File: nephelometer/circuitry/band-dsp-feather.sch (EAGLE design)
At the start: 63 parts, among them IC1 LM4041CILP, IC2 AD822N, IC3 MCP6S21, IC4 LP2950ACZ-3.3, J1 RJ11-6PTH, Q1 IRLB8721, T1 2N2222, T2 2N2222, T3 2N2222, T4 2N2222, T5 2N2222, T6 2N2222

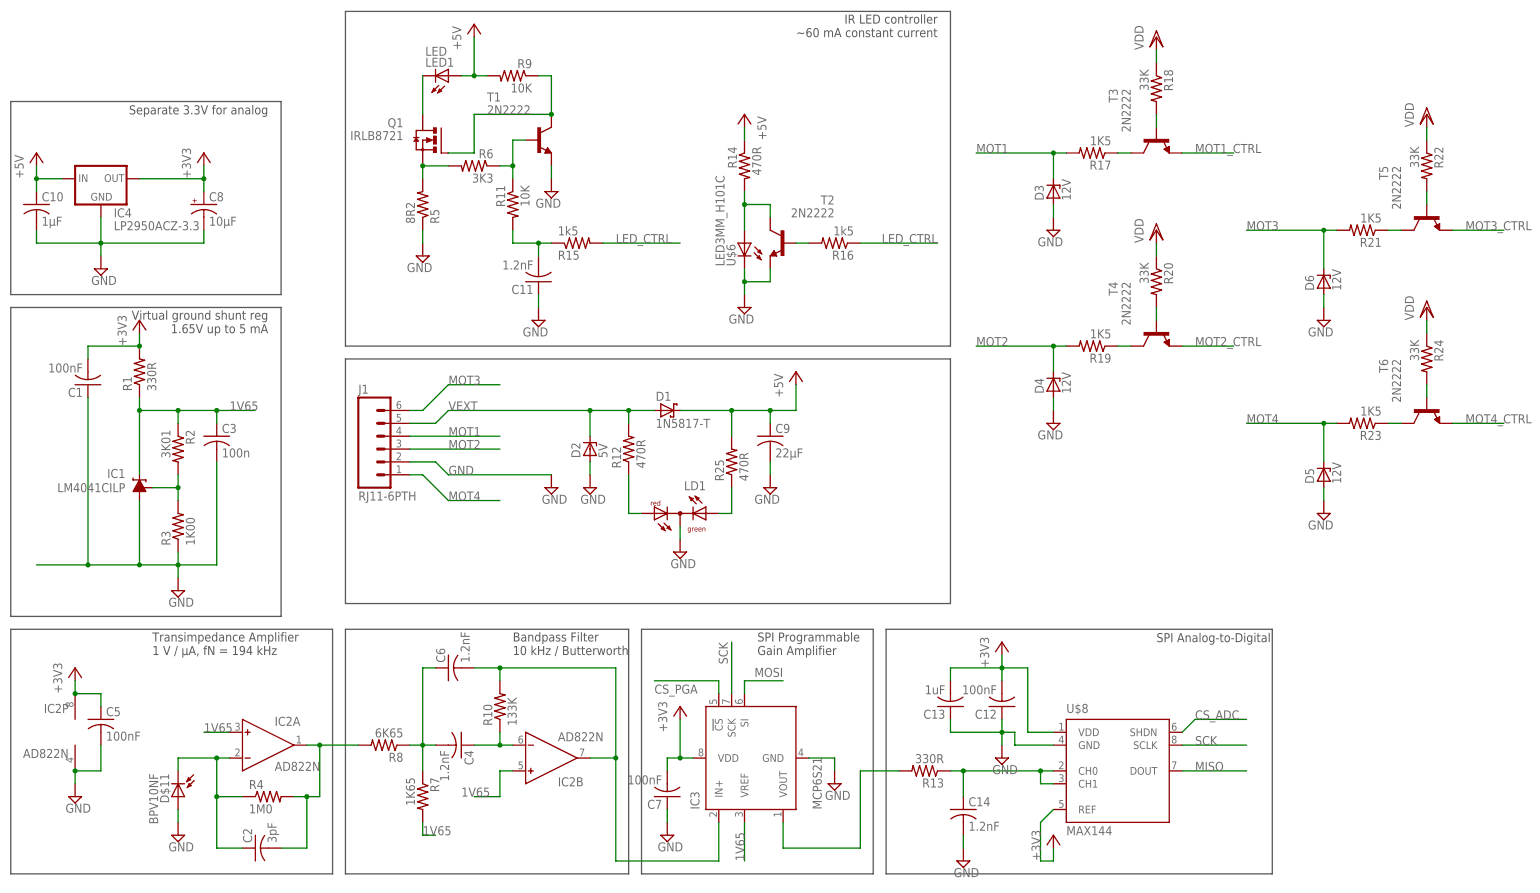
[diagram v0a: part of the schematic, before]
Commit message: Finalized Feather nephelometer with separate ADC and 4 robust motor controls
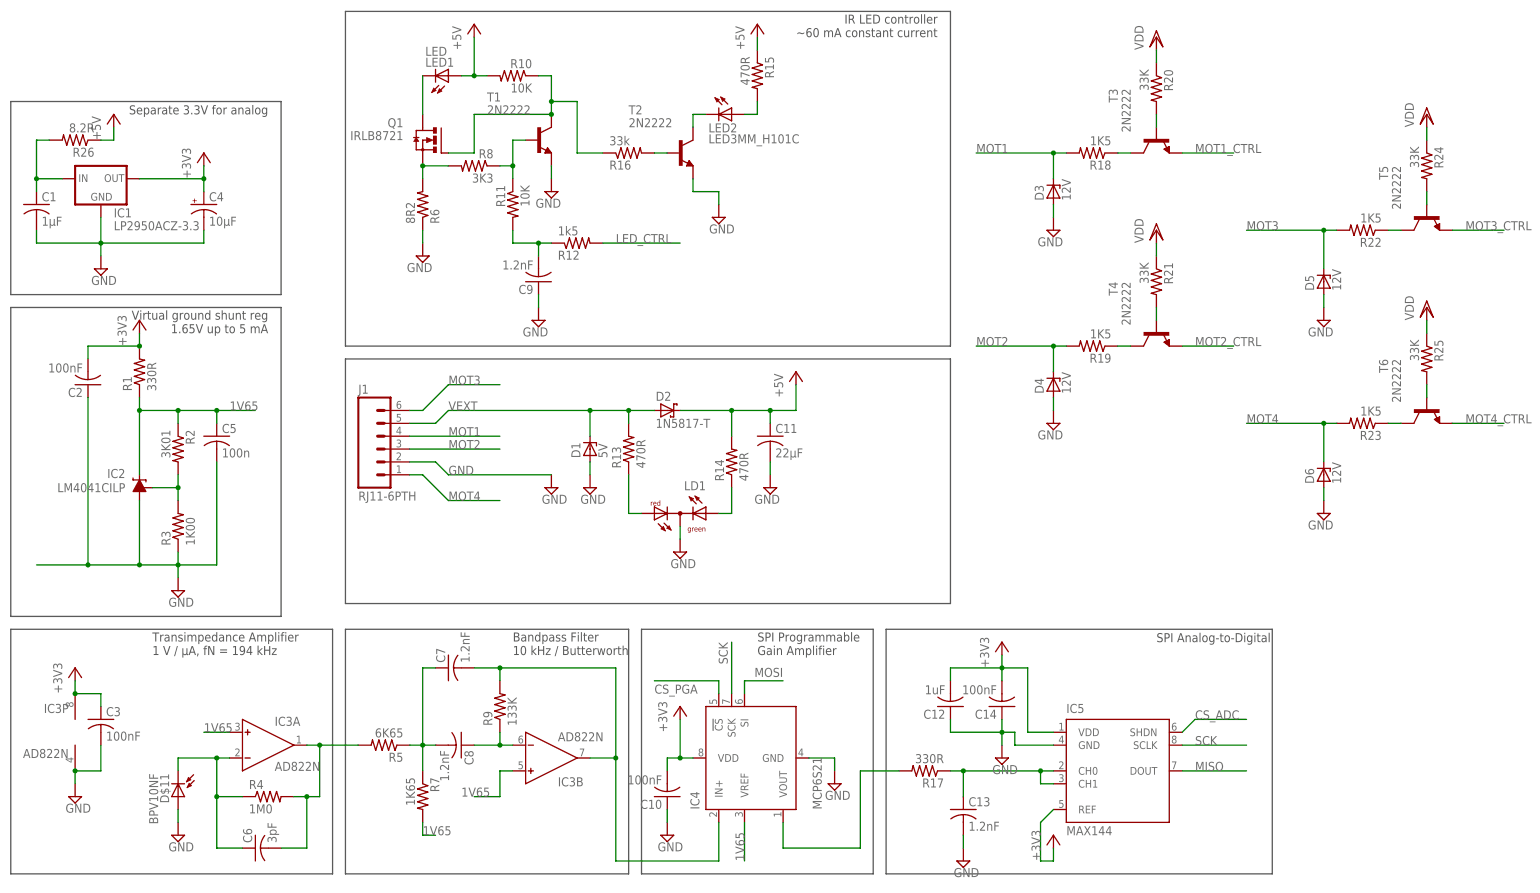
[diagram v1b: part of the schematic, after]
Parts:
- removed U$6: LED3MM_H101C, ingolia:LED3MM_H101C
- added LED2: LED3MM_H101C, ingolia:LED3MM_H101C
- added R26: 8.2R, adafruit:R-US_0207/9
- C1: value 100nF -> 1µF; device adafruit:C-US025-025X050 -> adafruit:C-US025-030X050; DIGIKEY# BC1084CT-ND -> 445-5318-ND; MANF Vishay BC Components -> TDK Corporation; MANF# K104K15X7RF5TL2 -> FK14X7R1C105K
- C10: value 1µF -> 100nF; device adafruit:C-US025-030X050 -> adafruit:C-US025-025X050; DIGIKEY# 445-5318-ND -> BC1084CT-ND; MANF TDK Corporation -> Vishay BC Components; MANF# FK14X7R1C105K -> K104K15X7RF5TL2
- C11: value 1.2nF -> 22µF; device adafruit:C-US025-025X050 -> adafruit:C-US050-045X075; DIGIKEY# BC1026CT-ND -> 445-8455-ND; MANF Vishay BC Components -> TDK Corporation; MANF# K122J15C0GF5TL2 -> FK20X7R1C226M
- C12: value 100nF -> 1uF; DIGIKEY# BC1084CT-ND -> 445-5318-ND; MANF Vishay BC Components -> TDK Corporation; MANF# K104K15X7RF5TL2 -> FK14X7R1C105K
- C13: value 1uF -> 1.2nF; DIGIKEY# BC1084CT-ND -> BC1026CT-ND; MANF# K104K15X7RF5TL2 -> K122J15C0GF5TL2
- C14: value 1.2nF -> 100nF; DIGIKEY# BC1026CT-ND -> BC1084CT-ND; MANF# K122J15C0GF5TL2 -> K104K15X7RF5TL2
- C2: value 3pF -> 100nF; device adafruit:C-US025-024X044 -> adafruit:C-US025-025X050; DIGIKEY# 445-8377-ND -> BC1084CT-ND; MANF TDK Corporation -> Vishay BC Components; MANF# FK18C0G1H030C -> K104K15X7RF5TL2
- C3: value 100n -> 100nF
- C4: value 1.2nF -> 10µF; device adafruit:C-US025-025X050 -> adafruit:CPOL-USE2.5-5; DIGIKEY# BC1026CT-ND -> 478-8042-1-ND; MANF Vishay BC Components -> AVX Corporation; MANF# K122J15C0GF5TL2 -> TAP106K016SRW
- C5: value 100nF -> 100n
- C6: value 1.2nF -> 3pF; device adafruit:C-US025-025X050 -> adafruit:C-US025-024X044; DIGIKEY# BC1026CT-ND -> 445-8377-ND; MANF Vishay BC Components -> TDK Corporation; MANF# K122J15C0GF5TL2 -> FK18C0G1H030C
- C7: value 100nF -> 1.2nF; DIGIKEY# BC1084CT-ND -> BC1026CT-ND; MANF# K104K15X7RF5TL2 -> K122J15C0GF5TL2
- C8: value 10µF -> 1.2nF; device adafruit:CPOL-USE2.5-5 -> adafruit:C-US025-025X050; DIGIKEY# 478-8042-1-ND -> BC1026CT-ND; MANF AVX Corporation -> Vishay BC Components; MANF# TAP106K016SRW -> K122J15C0GF5TL2
- C9: value 22µF -> 1.2nF; device adafruit:C-US050-045X075 -> adafruit:C-US025-025X050; DIGIKEY# 445-8455-ND -> BC1026CT-ND; MANF TDK Corporation -> Vishay BC Components; MANF# FK20X7R1C226M -> K122J15C0GF5TL2
- D1: value 1N5817-T -> 5V; device diode:1N5817-T -> diode:ZENER-DIODEF126-10; DIGIKEY# 1N5817FSCT-ND -> SA5.0ALFCT-ND; MANF Fairchild Semiconductor -> Littelfuse Inc.; MANF# 1N5817 -> SA5.0A
- D2: value 5V -> 1N5817-T; device diode:ZENER-DIODEF126-10 -> diode:1N5817-T; DIGIKEY# (none) -> 1N5817FSCT-ND; MANF (none) -> Fairchild Semiconductor; MANF# (none) -> 1N5817
- D3, D4, D5, D6: DIGIKEY# (none) -> SA12CALFCT-ND; MANF (none) -> Littelfuse Inc.; MANF# (none) -> SA12CA
- IC1: value LM4041CILP -> LP2950ACZ-3.3; device texas:LM4041CILP -> v-reg:LP2950ACZ-3.3; DIGIKEY# 296-22173-1-ND -> LP2950ACZ-3.3/NOPB-ND; MANF# LM4041CILPR -> LP2950ACZ-3.3/NOPB
- IC2: value AD822N -> LM4041CILP; device analog-devices:AD822N -> texas:LM4041CILP; DIGIKEY# AD823ANZ-ND -> 296-22173-1-ND; MANF Analog Devices Inc. -> Texas Instruments; MANF# AD823ANZ -> LM4041CILPR
- IC3: value MCP6S21 -> AD822N; device ingolia:MCP6S21 -> analog-devices:AD822N; DIGIKEY# MCP6S91-E/P-ND -> AD823ANZ-ND; MANF Microchip Technology -> Analog Devices Inc.; MANF# MCP6S91-E/P -> AD823ANZ
- IC4: value LP2950ACZ-3.3 -> MCP6S21; device v-reg:LP2950ACZ-3.3 -> ingolia:MCP6S21; DIGIKEY# LP2950ACZ-3.3/NOPB-ND -> MCP6S91-E/P-ND; MANF Texas Instruments -> Microchip Technology; MANF# LP2950ACZ-3.3/NOPB -> MCP6S91-E/P
- IC5: DIGIKEY# (none) -> MAX144ACPA+-ND; MANF (none) -> Maxim Integrated; MANF# (none) -> MAX144ACPA+
- IC6: DIGIKEY# (none) -> 1528-1531-ND; DIGIKEY2# (none) -> 2830-ND; MANF (none) -> Adafruit Industries LLC; MANF# (none) -> 2772; MANF2 (none) -> Adafruit Industries LLC; MANF2# (none) -> 2830
- LD1: DIGIKEY# (none) -> 754-1221-ND; MANF (none) -> Kingbright; MANF# (none) -> WP3VEGW
- R10: value 133K -> 10K; DIGIKEY# 133KXBK-ND -> CF14JT10K0CT-ND; MANF Yageo -> Stackpole Electronics Inc; MANF# MFR-25FBF52-133K -> CF14JT10K0
- R11: DIGIKEY# CF14JT4K70CT-ND -> CF14JT10K0CT-ND; MANF# CF14JT4K70 -> CF14JT10K0
- R12: value 470R -> 1k5; DIGIKEY# CF14JT330RCT-ND -> CF14JT1K50CT-ND; MANF Stackpole Electronics Inc. -> Stackpole Electronics Inc; MANF# CF14JT330R -> CF14JT1K50
- R13: value 330R -> 470R; DIGIKEY# 6.65KXBK-ND -> CF14JT470RCT-ND; MANF Yageo -> Stackpole Electronics Inc.; MANF# MFR-25FBF52-6K65 -> CF14JT470R
- R14: device adafruit:R-US_0207/5V -> adafruit:R-US_0207/9; DIGIKEY# CF14JT150RCT-ND -> CF14JT470RCT-ND; MANF# CF14JT150R -> CF14JT470R
- R15: value 1k5 -> 470R; device adafruit:R-US_0207/9 -> adafruit:R-US_0207/5V; DIGIKEY# CF14JT4K70CT-ND -> CF14JT470RCT-ND; MANF Stackpole Electronics Inc -> Stackpole Electronics Inc.; MANF# CF14JT4K70 -> CF14JT470R
- R16: value 1k5 -> 33k; DIGIKEY# CF14JT4K70CT-ND -> CF14JT33K0CT-ND; MANF# CF14JT4K70 -> CF14JT33K0
- R17: value 1K5 -> 330R; DIGIKEY# CF14JT330RCT-ND -> S330CACT-ND; MANF# CF14JT330R -> RNMF14FTC330R
- R18, R22: value 33K -> 1K5; DIGIKEY# CF14JT330RCT-ND -> CF14JT1K50CT-ND; MANF# CF14JT330R -> CF14JT1K50
- R19, R23: DIGIKEY# CF14JT330RCT-ND -> CF14JT1K50CT-ND; MANF# CF14JT330R -> CF14JT1K50
- R20, R24: DIGIKEY# CF14JT330RCT-ND -> CF14JT33K0CT-ND; MANF# CF14JT330R -> CF14JT33K0
- R21: value 1K5 -> 33K; DIGIKEY# CF14JT330RCT-ND -> CF14JT33K0CT-ND; MANF# CF14JT330R -> CF14JT33K0
- R25: value 470R -> 33K; DIGIKEY# CF14JT330RCT-ND -> CF14JT33K0CT-ND; MANF# CF14JT330R -> CF14JT33K0
- R5: value 8R2 -> 6K65; DIGIKEY# S8.2HCT-ND -> 6.65KXBK-ND; MANF Stackpole Electronics Inc. -> Yageo; MANF# CFM12JT8R20 -> MFR-25FBF52-6K65
- R6: value 3K3 -> 8R2; DIGIKEY# CF14JT4K70CT-ND -> S8.2HCT-ND; MANF Stackpole Electronics Inc -> Stackpole Electronics Inc.; MANF# CF14JT4K70 -> CFM12JT8R20
- R8: value 6K65 -> 3K3; DIGIKEY# 6.65KXBK-ND -> CF14JT3K30CT-ND; MANF Yageo -> Stackpole Electronics Inc; MANF# MFR-25FBF52-6K65 -> CF14JT3K30
- R9: value 10K -> 133K; DIGIKEY# CF14JT4K70CT-ND -> 133KXBK-ND; MANF Stackpole Electronics Inc -> Yageo; MANF# CF14JT4K70 -> MFR-25FBF52-133K
- renumbered U$7 to IC6, U$8 to IC5
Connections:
- new net N$12: LED2.K, T2.C
- new net N$24: C1.1, IC1.IN, R26.2
- net +3V3: now also C10.2, C14.2, C2.2, C3.1, C4.+, IC1.OUT, IC3P.V+, IC4.VDD; no longer C1.2, C13.2, C5.1, C7.2, C8.+, IC2P.V+, IC3.VDD, IC4.OUT
- net +5V: now also C11.1, D2.C, R10.2, R14.2, R15.1, R26.1; no longer C10.1, C9.1, D1.C, IC4.IN, R14.1, R25.2, R9.2
- net 1V65: now also C5.1, IC2.C, IC3A.IN+, IC3B.IN+, IC4.VREF; no longer C3.1, IC1.C, IC2A.IN+, IC2B.IN+, IC3.VREF
- net BPF: now also C7.2, IC3B.OUT, IC4.IN+, R9.2; no longer C6.2, IC2B.OUT, IC3.IN+, R10.2
- net CS_PGA: now also IC4.!CS; no longer IC3.!CS
- net FB: now also C6.1, IC3A.IN-; no longer C2.1, IC2A.IN-
- net GND: now also C1.2, C10.1, C11.2, C13.2, C14.1, C2.1, C4.-, C9.1, D1.A, IC1.GND, IC2.A, IC3P.V-, R6.1; no longer C1.1, C10.2, C11.1, C13.1, C14.2, C7.1, C8.-, C9.2, D2.A, IC1.A, IC2P.V-, IC3.GND, R5.1, U$6.K
- net LED_CTRL: now also R12.2; no longer R15.2, R16.1
- net MOSI: now also IC4.SI; no longer IC3.SI
- net MOT1: now also R18.2; no longer R17.2
- net MOT3: now also D5.C, R22.2; no longer D6.C, R21.2
- net MOT4: now also D6.C; no longer D5.C
- net N$11: now also LED2.A, R15.2; no longer R14.2, T2.C, U$6.A
- net N$13: now also R8.1; no longer R6.1
- net N$14: now also R8.2; no longer R5.2
- net N$15: now also C9.2, R12.1; no longer C11.2, R15.1
- net N$19: now also R18.1; no longer R17.1
- net N$2: now also R21.2; no longer R20.2
- net N$20: now also R20.2; no longer R18.2
- net N$21: now also R25.2; no longer R24.2
- net N$22: now also R13.1; no longer R12.1
- net N$23: now also C13.1, R17.1; no longer C14.1, R13.1
- net N$3: now also C7.1, C8.2, R5.1; no longer C4.2, C6.1, R8.1
- net N$35: now also IC2.FB; no longer IC1.FB
- net N$4: now also IC4.VOUT, R17.2; no longer IC3.VOUT, R13.2
- net N$5: now also R22.1; no longer R21.1
- net N$6: now also R24.2; no longer R22.2
- net N$7: now also R14.1; no longer R25.1
- net N$8: now also R10.1, R16.1; no longer R9.1
- net N$9: now also C8.1, IC3B.IN-, R9.1; no longer C4.1, IC2B.IN-, R10.1
- net SCK: now also IC4.SCK; no longer IC3.SCK
- net TIA: now also C6.2, IC3A.OUT, R5.2; no longer C2.2, IC2A.OUT, R8.2
- net VDD: now also R21.1, R25.1; no longer R18.1, R22.1
- net VEXT: now also D1.C, D2.A, R13.2; no longer D1.A, D2.C, R12.2
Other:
- moved on the sheet: C1, C10, C11, C12, C13, C14, C2, C3, C5, C6, C7, C9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

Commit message: Minor updates after test assembly
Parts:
- D3, D4, D5, D6: DIGIKEY# SA12CALFCT-ND -> SA12ALFCT-ND; MANF# SA12CA -> SA12A
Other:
- note added: "Bandpass Filter 10 kHz / -10x / Q = 5"
- note removed: "Bandpass Filter 10 kHz / Butterworth"
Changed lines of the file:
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@@
 <grid distance="0.1" unitdist="inch" unit="inch" style="lines" multiple="1" display="no" altdistance="0.01" altunitdist="inch" altunit="inch"/>
 <layers>
-<layer number="1" name="Top" color="4" fill="1" visible="yes" active="no"/>
-<layer number="16" name="Bottom" color="1" fill="1" visible="yes" active="no"/>
-<layer number="17" name="Pads" color="2" fill="1" visible="yes" active="no"/>
-<layer number="18" name="Vias" color="2" fill="1" visible="yes" active="no"/>
-<layer number="19" name="Unrouted" color="6" fill="1" visible="yes" active="no"/>
-<layer number="20" name="Dimension" color="15" fill="1" visible="yes" active="no"/>
-<layer number="21" name="tPlace" color="7" fill="1" visible="yes" active="no"/>
-<layer number="22" name="bPlace" color="7" fill="1" visible="yes" active="no"/>
-<layer number="23" name="tOrigins" color="15" fill="1" visible="yes" active="no"/>
-<layer number="24" name="bOrigins" color="15" fill="1" visible="yes" active="no"/>
-<layer number="25" name="tNames" color="7" fill="1" visible="yes" active="no"/>
-<layer number="26" name="bNames" color="7" fill="1" visible="yes" active="no"/>
-<layer number="27" name="tValues" color="7" fill="1" visible="yes" active="no"/>
-<layer number="28" name="bValues" color="7" fill="1" visible="yes" active="no"/>
+<layer number="1" name="Top" color="4" fill="1" visible="no" active="no"/>
+<layer number="16" name="Bottom" color="1" fill="1" visible="no" active="no"/>
+<layer number="17" name="Pads" color="2" fill="1" visible="no" active="no"/>
+<layer number="18" name="Vias" color="2" fill="1" visible="no" active="no"/>
+<layer number="19" name="Unrouted" color="6" fill="1" visible="no" active="no"/>
+<layer number="20" name="Dimension" color="15" fill="1" visible="no" active="no"/>
+<layer number="21" name="tPlace" color="7" fill="1" visible="no" active="no"/>
+<layer number="22" name="bPlace" color="7" fill="1" visible="no" active="no"/>
+<layer number="23" name="tOrigins" color="15" fill="1" visible="no" active="no"/>
+<layer number="24" name="bOrigins" color="15" fill="1" visible="no" active="no"/>
+<layer number="25" name="tNames" color="7" fill="1" visible="no" active="no"/>
+<layer number="26" name="bNames" color="7" fill="1" visible="no" active="no"/>
+<layer number="27" name="tValues" color="7" fill="1" visible="no" active="no"/>
+<layer number="28" name="bValues" color="7" fill="1" visible="no" active="no"/>
 <layer number="29" name="tStop" color="7" fill="3" visible="no" active="no"/>
 <layer number="30" name="bStop" color="7" fill="6" visible="no" active="no"/>
@@
 <layer number="35" name="tGlue" color="7" fill="4" visible="no" active="no"/>
 <layer number="36" name="bGlue" color="7" fill="5" visible="no" active="no"/>
-<layer number="37" name="tTest" color="7" fill="1" visible="yes" active="no"/>
-<layer number="38" name="bTest" color="7" fill="1" visible="yes" active="no"/>
+<layer number="37" name="tTest" color="7" fill="1" visible="no" active="no"/>
+<layer number="38" name="bTest" color="7" fill="1" visible="no" active="no"/>
 <layer number="39" name="tKeepout" color="4" fill="11" visible="no" active="no"/>
 <layer number="40" name="bKeepout" color="1" fill="11" visible="no" active="no"/>
@@
 <layer number="44" name="Drills" color="7" fill="1" visible="no" active="no"/>
 <layer number="45" name="Holes" color="7" fill="1" visible="no" active="no"/>
-<layer number="46" name="Milling" color="3" fill="1" visible="yes" active="no"/>
-<layer number="47" name="Measures" color="7" fill="1" visible="yes" active="no"/>
-<layer number="48" name="Document" color="7" fill="1" visible="yes" active="no"/>
-<layer number="49" name="Reference" color="7" fill="1" visible="yes" active="no"/>
-<layer number="50" name="dxf" color="7" fill="1" visible="yes" active="no"/>
-<layer number="51" name="tDocu" color="7" fill="1" visible="yes" active="no"/>
-<layer number="52" name="bDocu" color="7" fill="1" visible="yes" active="no"/>
-<layer number="53" name="tGND_GNDA" color="7" fill="9" visible="yes" active="no"/>
-<layer number="54" name="bGND_GNDA" color="1" fill="9" visible="yes" active="no"/>
-<layer number="56" name="wert" color="7" fill="1" visible="yes" active="no"/>
-<layer number="57" name="tCAD" color="7" fill="1" visible="yes" active="no"/>
-<layer number="59" name="tCarbon" color="7" fill="1" visible="yes" active="no"/>
-<layer number="60" name="bCarbon" color="7" fill="1" visible="yes" active="no"/>
+<layer number="46" name="Milling" color="3" fill="1" visible="no" active="no"/>
+<layer number="47" name="Measures" color="7" fill="1" visible="no" active="no"/>
+<layer number="48" name="Document" color="7" fill="1" visible="no" active="no"/>
+<layer number="49" name="Reference" color="7" fill="1" visible="no" active="no"/>
+<layer number="50" name="dxf" color="7" fill="1" visible="no" active="no"/>
+<layer number="51" name="tDocu" color="7" fill="1" visible="no" active="no"/>
+<layer number="52" name="bDocu" color="7" fill="1" visible="no" active="no"/>
+<layer number="53" name="tGND_GNDA" color="7" fill="9" visible="no" active="no"/>
+<layer number="54" name="bGND_GNDA" color="1" fill="9" visible="no" active="no"/>
+<layer number="56" name="wert" color="7" fill="1" visible="no" active="no"/>
+<layer number="57" name="tCAD" color="7" fill="1" visible="no" active="no"/>
+<layer number="59" name="tCarbon" color="7" fill="1" visible="no" active="no"/>
+<layer number="60" name="bCarbon" color="7" fill="1" visible="no" active="no"/>
 <layer number="90" name="Modules" color="5" fill="1" visible="yes" active="yes"/>
 <layer number="91" name="Nets" color="2" fill="1" visible="yes" active="yes"/>
@@
 <part name="SUPPLY15" library="supply2" deviceset="GND" device=""/>
 <part name="D3" library="diode" deviceset="ZENER-DIODE" device="F126-10" value="12V">
-<attribute name="DIGIKEY#" value="SA12CALFCT-ND"/>
+<attribute name="DIGIKEY#" value="SA12ALFCT-ND"/>
 <attribute name="MANF" value="Littelfuse Inc."/>
-<attribute name="MANF#" value="SA12CA"/>
+<attribute name="MANF#" value="SA12A"/>
 </part>
 <part name="SUPPLY17" library="supply2" deviceset="GND" device=""/>
 <part name="D4" library="diode" deviceset="ZENER-DIODE" device="F126-10" value="12V">
-<attribute name="DIGIKEY#" value="SA12CALFCT-ND"/>
+<attribute name="DIGIKEY#" value="SA12ALFCT-ND"/>
 <attribute name="MANF" value="Littelfuse Inc."/>
-<attribute name="MANF#" value="SA12CA"/>
+<attribute name="MANF#" value="SA12A"/>
 </part>
 <part name="SUPPLY18" library="supply2" deviceset="GND" device=""/>
 <part name="D6" library="diode" deviceset="ZENER-DIODE" device="F126-10" value="12V">
-<attribute name="DIGIKEY#" value="SA12CALFCT-ND"/>
+<attribute name="DIGIKEY#" value="SA12ALFCT-ND"/>
 <attribute name="MANF" value="Littelfuse Inc."/>
-<attribute name="MANF#" value="SA12CA"/>
+<attribute name="MANF#" value="SA12A"/>
 </part>
 <part name="SUPPLY20" library="supply2" deviceset="GND" device=""/>
 <part name="D5" library="diode" deviceset="ZENER-DIODE" device="F126-10" value="12V">
-<attribute name="DIGIKEY#" value="SA12CALFCT-ND"/>
+<attribute name="DIGIKEY#" value="SA12ALFCT-ND"/>
 <attribute name="MANF" value="Littelfuse Inc."/>
-<attribute name="MANF#" value="SA12CA"/>
+<attribute name="MANF#" value="SA12A"/>
 </part>
 <part name="SUPPLY19" library="supply2" deviceset="GND" device=""/>
@@
 <wire x1="111.76" y1="22.86" x2="167.64" y2="22.86" width="0.1524" layer="97"/>
 <wire x1="167.64" y1="71.12" x2="167.64" y2="22.86" width="0.1524" layer="97"/>
-<text x="144.78" y="66.04" size="1.778" layer="97">Bandpass Filter
-10 kHz / Butterworth</text>
+<text x="112.268" y="23.876" size="1.778" layer="97">Bandpass Filter
+10 kHz / -10x / Q = 5</text>
 <wire x1="45.72" y1="134.62" x2="45.72" y2="73.66" width="0.1524" layer="97"/>
 <wire x1="45.72" y1="73.66" x2="99.06" y2="73.66" width="0.1524" layer="97"/>
